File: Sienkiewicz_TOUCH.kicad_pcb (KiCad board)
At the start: 2 copper layers, 38 x 38 mm, 24 parts, among them J1 TC2030-NL, J2 USB4135-GF-A, U1 ATtiny204-SS, U2 AT42QT1012

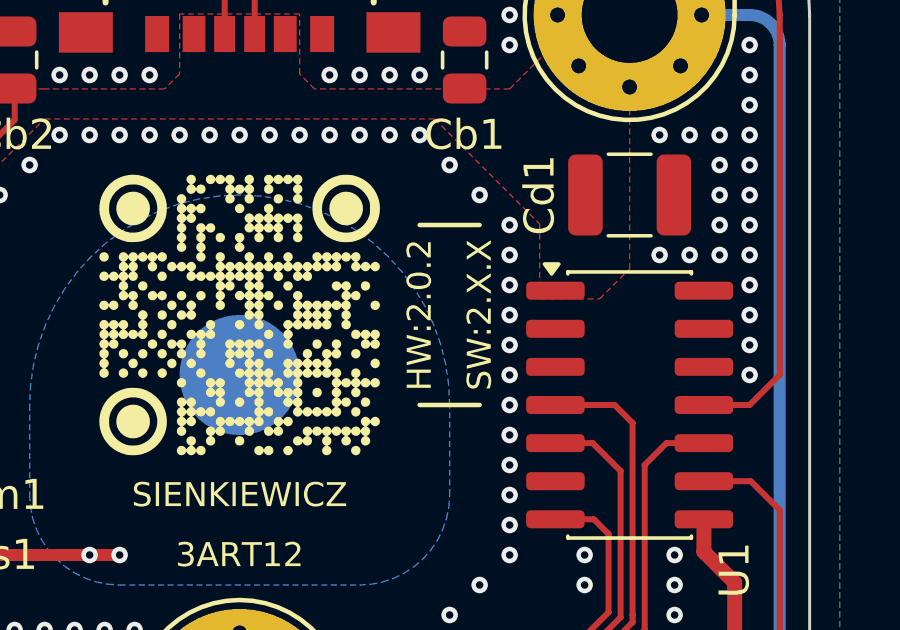
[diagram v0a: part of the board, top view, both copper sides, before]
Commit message: initial prep for SR signals reassignment (refs #4)
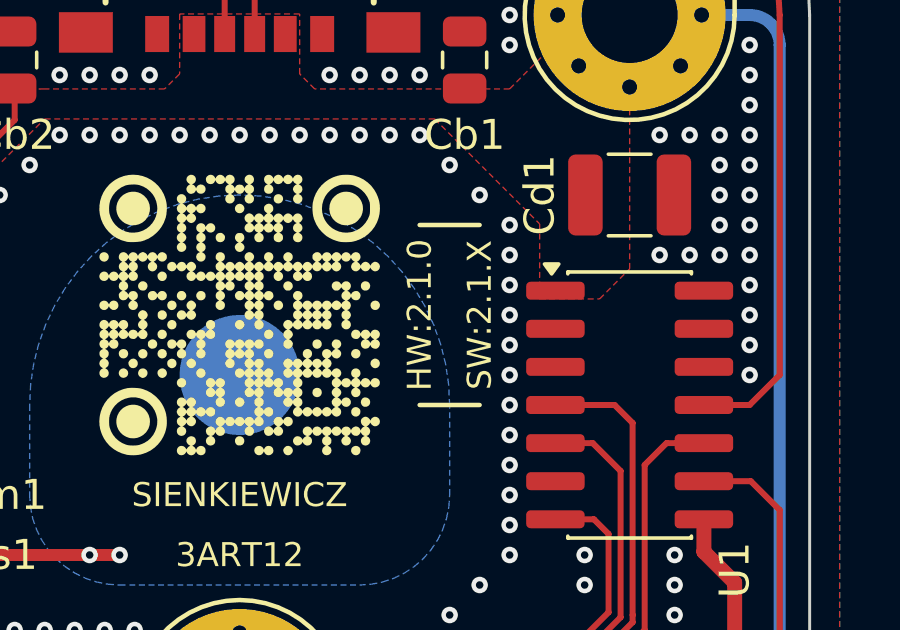
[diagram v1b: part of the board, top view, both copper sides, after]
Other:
- board text added: "HW:2.1.0"
- board text added: "SW:2.1.X"
- board text removed: "HW:2.0.2"
- board text removed: "SW:2.X.X"
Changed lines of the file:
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@@
 	(property "DESIGNER" "Pawel Baran")
 	(property "FABRICATION_NOTES" "FABRICATION NOTES (UNLESS OTHERWISE SPECIFIED)\n\n1)	FABRICATE PER IPC-6012A CLASS 2.\n\n2)	OUTLINE DEFINED IN SEPARATE GERBER FILE WITH\n	\"Edge_Cuts.GBR\" SUFFIX.\n\n	DIMENSIONS OF CIRCUMSIZED RECTANGLE SHOWN ON THIS\n	DRAWING FOR REFERENCE ONLY.\n\n3)	SEE SEPARATE DRILL FILES WITH \".DRL\" SUFFIX \n	FOR HOLE LOCATIONS.\n\n	SELECTED HOLE LOCATIONS SHOWN ON THIS DRAWING \n	FOR REFERENCE ONLY.\n\n4)	SURFACE FINISH: IMMERSION GOLD\n\n5)	SOLDERMASK ON BOTH SIDES OF THE BOARD SHALL \n	BE LPI, COLOR BLACK.\n\n6)	SILK SCREEN LEGEND TO BE APPLIED PER LAYER \n	STACKUP USING YELLOW NON-CONDUCTIVE EPOXY INK.\n\n7)	ALL VIAS ARE TENTED ON BOTH SIDES UNLESS \n	SOLDERMASK OPENED IN GERBER.\n\n8)	VENDOR SHOULD FOLLOW ROHS COMPLIANT PROCESS \n	AND Pb FREE FOR MANUFACTURING\n\n9)	PCB MATERIAL REQUIREMENTS:\n\n	A.	FLAMMABILITY RATING MUST MEET OR EXCEED \n		UL94V-0 REQUIREMENTS.\n	B.	Tg 170 C OR EQUIVALENT.\n	C.	EQUIVALENT MATERIAL SHALL BE RoHS COMPLIANT, \n		HALOGEN FREE AND APPROVED BY BAJRAN IMGAGINARY INDUSTRIES.\n\n10)	DESIGN GEOMETRY MINIMUM FEATURE SIZES:\n\n	BOARD SIZE				38.000 × 38.000 mm\n	BOARD THICKNESS		1.660 mm\n	TRACE WIDTH			0.200 mm\n	TRACE TO TRACE		-0.000 mm\n	MIN. HOLE (PTH)			0.250 mm\n	MIN. HOLE (NPTH)		1.000 mm\n	ANNULAR RING			0.150 mm\n	COPPER TO HOLE		0.254 mm\n	COPPER TO EDGE		0.250 mm\n	HOLE TO HOLE			0.254 mm\n\n11)	REFER TO IMPEDANCE TABLE FOR IMPEDANCE CONTROL REQUIREMENTS.\n\n12)	CONFIRM SPACE WIDTHS AND SPACINGS.")
-	(property "GIT_HASH_PCB" "05ded56")
+	(property "GIT_HASH_PCB" "a82ce84")
 	(property "GIT_HASH_SCH" "6405aa0")
 	(property "GIT_URL" "https://github.com/nguyen-v/KDT_Hierarchical_KiBot")
@@
 	(property "RELEASE_BODY_2.0.2" "Version 2.0.2 not found.")
 	(property "RELEASE_BODY_UNRELEASED" "Version Unreleased not found.")
-	(property "RELEASE_DATE" "25-Apr-2026")
-	(property "RELEASE_DATE_NUM" "2026-04-25")
+	(property "RELEASE_DATE" "27-Apr-2026")
+	(property "RELEASE_DATE_NUM" "2026-04-27")
 	(property "RELEASE_TITLE_1.0.0" "")
 	(property "RELEASE_TITLE_1.0.1" "")
@@
 		)
 	)
-	(gr_text "HW:2.0.2"
+	(gr_text "HW:2.1.0"
 		(at 154.5 87 90)
 		(layer "F.SilkS")
@@
 		)
 	)
-	(gr_text "SW:2.X.X"
+	(gr_text "SW:2.1.X"
 		(at 156.5 87 90)
 		(layer "F.SilkS")

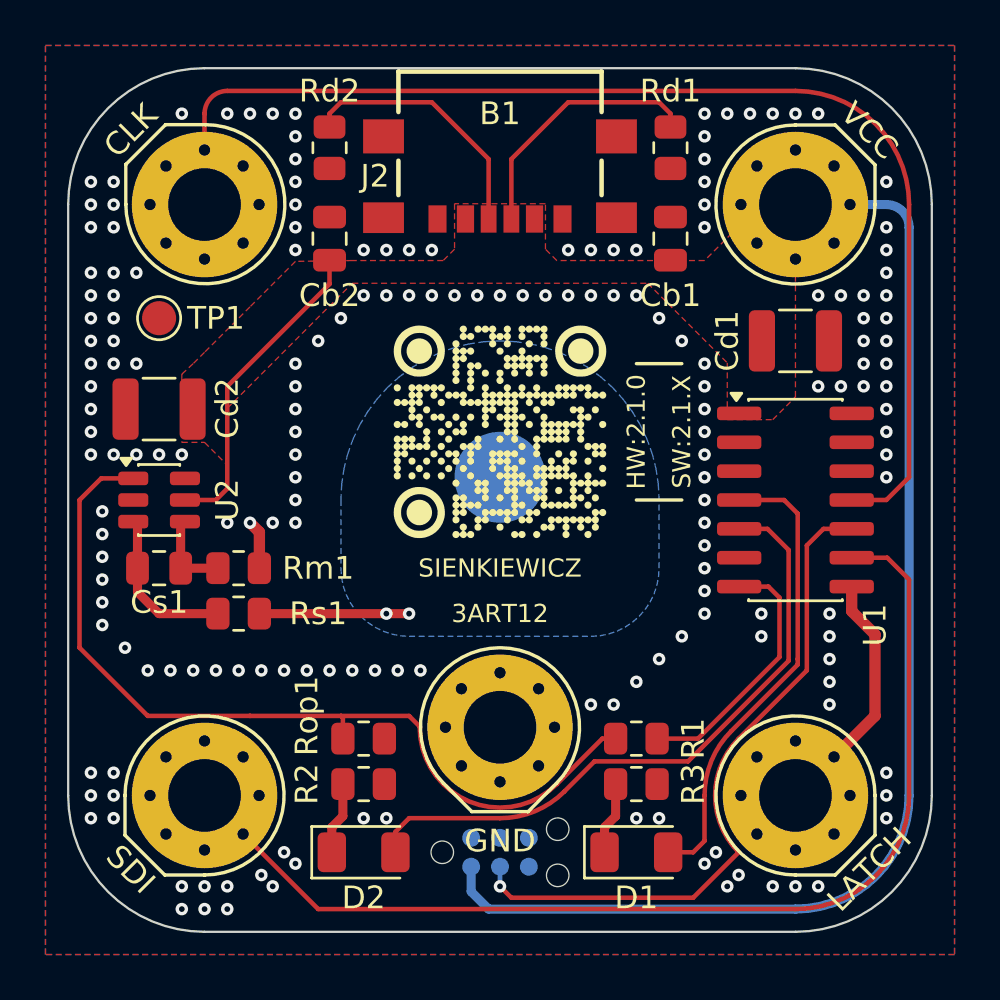
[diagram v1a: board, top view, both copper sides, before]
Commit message: reassign SR signals for clean design (fixes #4)
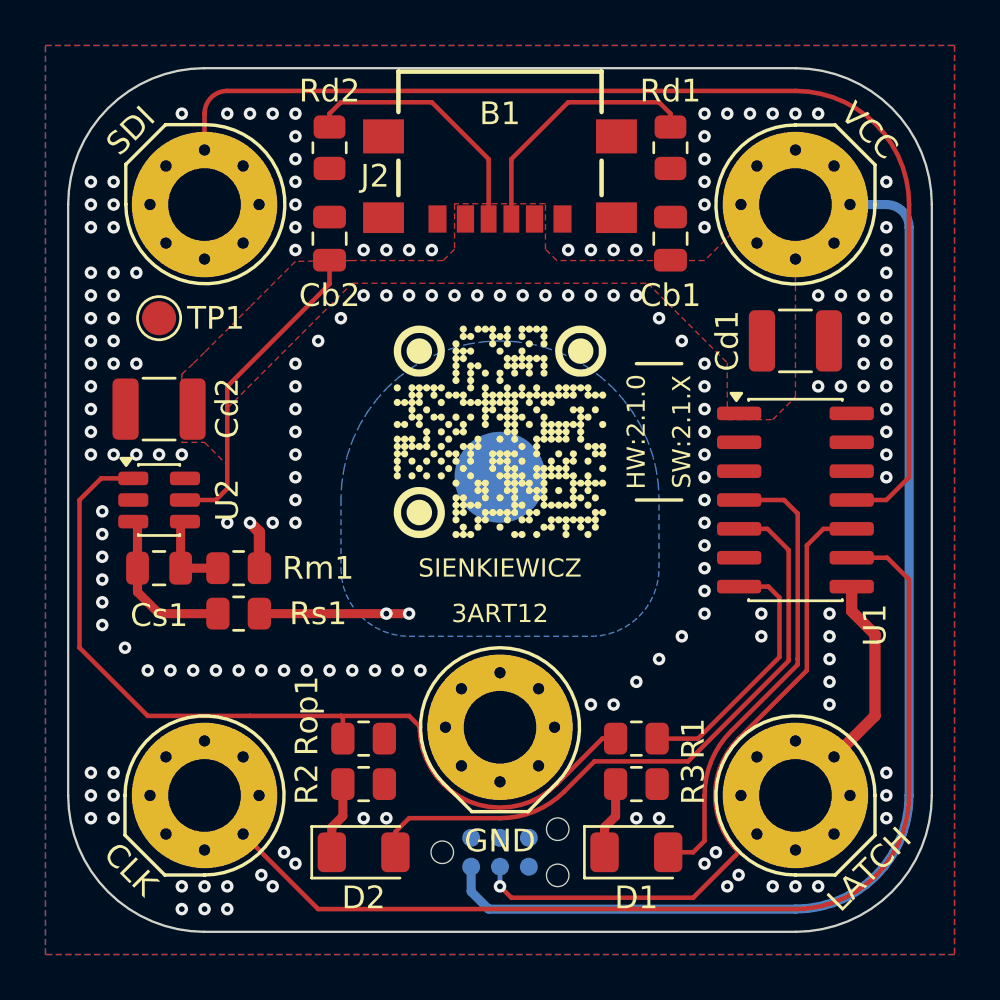
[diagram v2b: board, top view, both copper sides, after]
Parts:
- J1: value TC2030-NL -> Conn_ARM_SWD_TagConnect_TC2030-NL
- J2: value USB4135-GF-A -> USB4135-GF-A_REVA
- U2: value AT42QT1012 -> AT42QT1012-T
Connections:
- B1 pad 1: /Project Architecture/Section B - uC/SR_CLK -> /Project Architecture/Section B - uC/SR_SDI
- B1 pad 4: /Project Architecture/Section B - uC/SR_SDI -> /Project Architecture/Section B - uC/SR_CLK
- U1 pad 11: /Project Architecture/Section B - uC/SR_CLK -> /Project Architecture/Section B - uC/SR_SDI
- U1 pad 9: /Project Architecture/Section B - uC/SR_SDI -> /Project Architecture/Section B - uC/SR_CLK
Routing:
- net /Project Architecture/Section B - uC/SR_SDI: track 42.0 -> 43.9 mm
- net /Project Architecture/Section B - uC/SR_CLK: track 43.9 -> 42.0 mm
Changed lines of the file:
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@@
 			(layers "F.Cu" "F.Mask" "F.Paste")
 			(roundrect_rratio 0.25)
-			(net 16 "/Project Architecture/Section B - uC/SR_SDI")
+			(net 24 "/Project Architecture/Section B - uC/SR_CLK")
 			(pinfunction "PB0")
 			(pintype "bidirectional")
@@
 			(layers "F.Cu" "F.Mask" "F.Paste")
 			(roundrect_rratio 0.25)
-			(net 24 "/Project Architecture/Section B - uC/SR_CLK")
+			(net 16 "/Project Architecture/Section B - uC/SR_SDI")
 			(pinfunction "PA1")
 			(pintype "bidirectional")
@@
 			(layers "*.Cu" "*.Mask")
 			(remove_unused_layers no)
-			(net 24 "/Project Architecture/Section B - uC/SR_CLK")
-			(pinfunction "CLK")
+			(net 16 "/Project Architecture/Section B - uC/SR_SDI")
+			(pinfunction "SDI")
 			(pintype "bidirectional")
 			(zone_connect 2)
@@
 			(layers "*.Cu" "*.Mask")
 			(remove_unused_layers no)
-			(net 24 "/Project Architecture/Section B - uC/SR_CLK")
-			(pinfunction "CLK")
+			(net 16 "/Project Architecture/Section B - uC/SR_SDI")
+			(pinfunction "SDI")
 			(pintype "bidirectional")
 			(zone_connect 2)
@@
 			(layers "*.Cu" "*.Mask")
 			(remove_unused_layers no)
-			(net 24 "/Project Architecture/Section B - uC/SR_CLK")
-			(pinfunction "CLK")
+			(net 16 "/Project Architecture/Section B - uC/SR_SDI")
+			(pinfunction "SDI")
 			(pintype "bidirectional")
 			(zone_connect 2)
@@
 			(layers "*.Cu" "*.Mask")
 			(remove_unused_layers no)
-			(net 24 "/Project Architecture/Section B - uC/SR_CLK")
-			(pinfunction "CLK")
+			(net 16 "/Project Architecture/Section B - uC/SR_SDI")
+			(pinfunction "SDI")
 			(pintype "bidirectional")
 			(zone_connect 2)
@@
 			(layers "*.Cu" "*.Mask")
 			(remove_unused_layers no)
-			(net 24 "/Project Architecture/Section B - uC/SR_CLK")
-			(pinfunction "CLK")
+			(net 16 "/Project Architecture/Section B - uC/SR_SDI")
+			(pinfunction "SDI")
 			(pintype "bidirectional")
 			(zone_connect 2)
@@
 			(layers "*.Cu" "*.Mask")
 			(remove_unused_layers no)
-			(net 24 "/Project Architecture/Section B - uC/SR_CLK")
-			(pinfunction "CLK")
+			(net 16 "/Project Architecture/Section B - uC/SR_SDI")
+			(pinfunction "SDI")
 			(pintype "bidirectional")
 			(zone_connect 2)
@@
 			(layers "*.Cu" "*.Mask")
 			(remove_unused_layers no)
-			(net 24 "/Project Architecture/Section B - uC/SR_CLK")
-			(pinfunction "CLK")
+			(net 16 "/Project Architecture/Section B - uC/SR_SDI")
+			(pinfunction "SDI")
 			(pintype "bidirectional")
 			(zone_connect 2)
@@
 			(layers "*.Cu" "*.Mask")
 			(remove_unused_layers no)
-			(net 24 "/Project Architecture/Section B - uC/SR_CLK")
-			(pinfunction "CLK")
+			(net 16 "/Project Architecture/Section B - uC/SR_SDI")
+			(pinfunction "SDI")
 			(pintype "bidirectional")
 			(zone_connect 2)
@@
 			(layers "*.Cu" "*.Mask")
 			(remove_unused_layers no)
-			(net 24 "/Project Architecture/Section B - uC/SR_CLK")
-			(pinfunction "CLK")
+			(net 16 "/Project Architecture/Section B - uC/SR_SDI")
+			(pinfunction "SDI")
 			(pintype "bidirectional")
 			(zone_connect 2)
@@
 			(layers "*.Cu" "*.Mask")
 			(remove_unused_layers no)
-			(net 16 "/Project Architecture/Section B - uC/SR_SDI")
-			(pinfunction "SDI")
+			(net 24 "/Project Architecture/Section B - uC/SR_CLK")
+			(pinfunction "CLK")
 			(pintype "bidirectional")
 			(zone_connect 2)
@@
 			(layers "*.Cu" "*.Mask")
 			(remove_unused_layers no)
-			(net 16 "/Project Architecture/Section B - uC/SR_SDI")
-			(pinfunction "SDI")
+			(net 24 "/Project Architecture/Section B - uC/SR_CLK")
+			(pinfunction "CLK")
 			(pintype "bidirectional")
 			(zone_connect 2)
@@
 			(layers "*.Cu" "*.Mask")
 			(remove_unused_layers no)
-			(net 16 "/Project Architecture/Section B - uC/SR_SDI")
-			(pinfunction "SDI")
+			(net 24 "/Project Architecture/Section B - uC/SR_CLK")
+			(pinfunction "CLK")
 			(pintype "bidirectional")
 			(zone_connect 2)
@@
 			(layers "*.Cu" "*.Mask")
 			(remove_unused_layers no)
-			(net 16 "/Project Architecture/Section B - uC/SR_SDI")
-			(pinfunction "SDI")
+			(net 24 "/Project Architecture/Section B - uC/SR_CLK")
+			(pinfunction "CLK")
 			(pintype "bidirectional")
 			(zone_connect 2)
@@
 			(layers "*.Cu" "*.Mask")
 			(remove_unused_layers no)
-			(net 16 "/Project Architecture/Section B - uC/SR_SDI")
-			(pinfunction "SDI")
+			(net 24 "/Project Architecture/Section B - uC/SR_CLK")
+			(pinfunction "CLK")
 			(pintype "bidirectional")
 			(zone_connect 2)
@@
 			(layers "*.Cu" "*.Mask")
 			(remove_unused_layers no)
-			(net 16 "/Project Architecture/Section B - uC/SR_SDI")
-			(pinfunction "SDI")
+			(net 24 "/Project Architecture/Section B - uC/SR_CLK")
+			(pinfunction "CLK")
 			(pintype "bidirectional")
 			(zone_connect 2)
@@
 			(layers "*.Cu" "*.Mask")
 			(remove_unused_layers no)
-			(net 16 "/Project Architecture/Section B - uC/SR_SDI")
-			(pinfunction "SDI")
+			(net 24 "/Project Architecture/Section B - uC/SR_CLK")
+			(pinfunction "CLK")
 			(pintype "bidirectional")
 			(zone_connect 2)
@@
 			(layers "*.Cu" "*.Mask")
 			(remove_unused_layers no)
-			(net 16 "/Project Architecture/Section B - uC/SR_SDI")
-			(pinfunction "SDI")
+			(net 24 "/Project Architecture/Section B - uC/SR_CLK")
+			(pinfunction "CLK")
 			(pintype "bidirectional")
 			(zone_connect 2)
@@
 			(layers "*.Cu" "*.Mask")
 			(remove_unused_layers no)
-			(net 16 "/Project Architecture/Section B - uC/SR_SDI")
-			(pinfunction "SDI")
+			(net 24 "/Project Architecture/Section B - uC/SR_CLK")
+			(pinfunction "CLK")
 			(pintype "bidirectional")
 			(zone_connect 2)
@@
 		(tags "capacitor")
 		(property "Reference" "Cs1"
-			(at 0 1.5 180)
+			(at 0 2.08 180)
 			(layer "F.SilkS")
 			(effects
@@
 			)
 		)
-		(property "Value" "USB4135-GF-A"
+		(property "Value" "USB4135-GF-A_REVA"
 			(at 0 -5.5 0)
 			(layer "F.Fab")
@@
 			)
 		)
-		(property "Value" "AT42QT1012"
+		(property "Value" "AT42QT1012-T"
 			(at 5 -4 270)
 			(layer "F.Fab")
@@
 			)
 		)
-		(property "Value" "TC2030-NL"
+		(property "Value" "Conn_ARM_SWD_TagConnect_TC2030-NL"
 			(at 0 -3.5 0)
 			(layer "B.Fab")
@@
 		)
 		(layer "F.Cu")
-		(net 24)
+		(net 16)
 	)
 	(gr_arc
@@
 		)
 		(layer "F.Cu")
-		(net 24)
+		(net 16)
 	)
 	(gr_arc
@@
 		)
 		(layer "F.Cu")
-		(net 16)
+		(net 24)
 	)
 	(gr_arc
@@
 		(layer "User.9")
 	)
-	(gr_text "CLK"
+	(gr_text "SDI"
 		(at 132.25 73.75 45)
 		(layer "F.SilkS" knockout)
@@
 		)
 	)
-	(gr_text "SDI"
+	(gr_text "CLK"
 		(at 132.25 106.25 315)
 		(layer "F.SilkS" knockout)
@@
 	)
 	(segment
-		(start 163.975 92.54)
-		(end 165.54 92.54)
-		(width 0.2)
-		(layer "F.Cu")
-		(net 16)
-	)
-	(segment
-		(start 166.5 93.5)
-		(end 166.5 103)
+		(start 163.975 90)
+		(end 165.5 90)
 		(width 0.2)
 		(layer "F.Cu")
@@
 	)
 	(segment
-		(start 137 103)
-		(end 135.5 103)
+		(start 166.5 89)
+		(end 166.5 77)
 		(width 0.2)
 		(layer "F.Cu")
@@
 	)
 	(segment
-		(start 140.5 108)
-		(end 135.5 103)
+		(start 161.5 72)
+		(end 136.5 72)
 		(width 0.2)
 		(layer "F.Cu")
@@
 	)
 	(segment
-		(start 165.54 92.54)
-		(end 166.5 93.5)
+		(start 135.5 73)
+		(end 135.5 77)
 		(width 0.2)
 		(layer "F.Cu")
@@
 	)
 	(segment
-		(start 161.5 108)
-		(end 140.5 108)
+		(start 165.5 90)
+		(end 166.5 89)
 		(width 0.2)
 		(layer "F.Cu")
@@
 	)
 	(segment
-		(start 163.975 90)
-		(end 165.5 90)
+		(start 163.975 92.54)
+		(end 165.54 92.54)
 		(width 0.2)
 		(layer "F.Cu")
@@
 	)
 	(segment
-		(start 166.5 89)
-		(end 166.5 77)
+		(start 166.5 93.5)
+		(end 166.5 103)
 		(width 0.2)
 		(layer "F.Cu")
@@
 	)
 	(segment
-		(start 161.5 72)
-		(end 136.5 72)
+		(start 137 103)
+		(end 135.5 103)
 		(width 0.2)
 		(layer "F.Cu")
@@
 	)
 	(segment
-		(start 135.5 73)
-		(end 135.5 77)
+		(start 140.5 108)
+		(end 135.5 103)
 		(width 0.2)
 		(layer "F.Cu")
@@
 	)
 	(segment
-		(start 165.5 90)
-		(end 166.5 89)
+		(start 165.54 92.54)
+		(end 166.5 93.5)
+		(width 0.2)
+		(layer "F.Cu")
+		(net 24)
+	)
+	(segment
+		(start 161.5 108)
+		(end 140.5 108)
 		(width 0.2)
 		(layer "F.Cu")

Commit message: Update Outputs (release)
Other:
- board text added: "B.Cu"
- board text added: "F.Cu"
- board text removed: "L1 (Sig, PWR)"
- board text removed: "L6 (Sig, PWR)"

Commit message: documentation update / block diagram
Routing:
- net /Project Architecture/Section B - uC/UPDI: track 25.7 -> 24.4 mm
